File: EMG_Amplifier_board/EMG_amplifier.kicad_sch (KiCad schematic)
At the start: 8 parts, among them J1 Conn_01x04_Socket, J2 Conn_01x04_Pin, J3 Conn_01x06_Pin, J4 Conn_01x06_Socket, J7 Conn_01x06_Pin

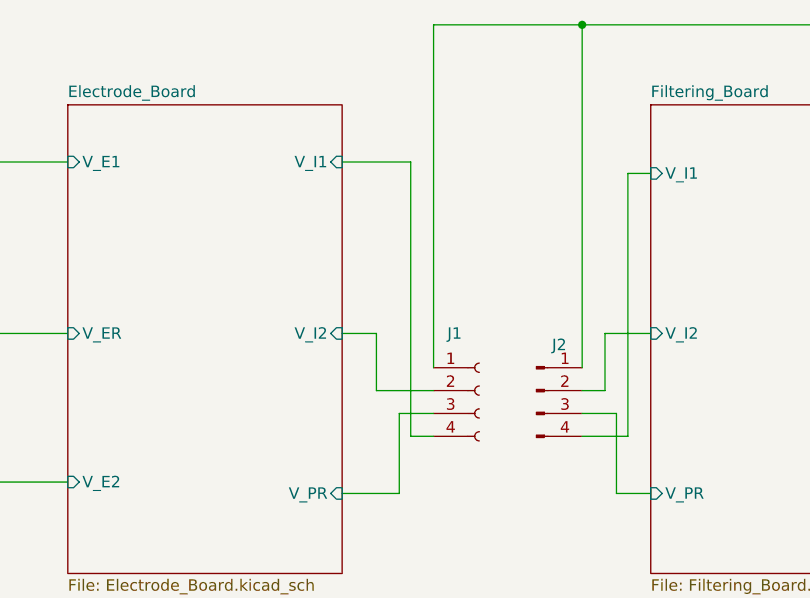
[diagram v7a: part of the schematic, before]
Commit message: correct the 400Hz LPF schematic and InAmp trace routing
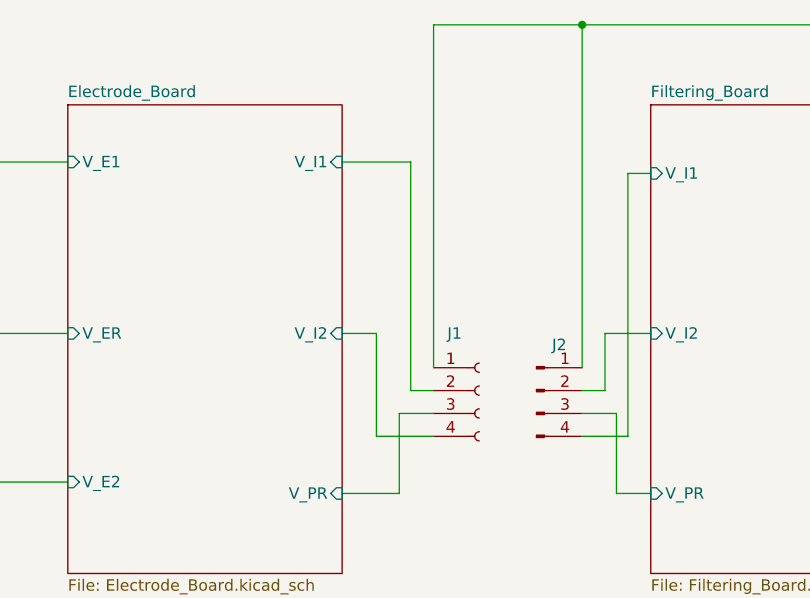
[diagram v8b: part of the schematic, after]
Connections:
- net Electrode_Board/V_I1: now also J1.2 (Pin_2); no longer J1.4 (Pin_4)
- net Electrode_Board/V_I2: now also J1.4 (Pin_4); no longer J1.2 (Pin_2)
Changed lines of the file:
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@@
+	(wire
+		(pts
+			(xy 95.25 69.85) (xy 95.25 95.25)
+		)
+		(stroke
+			(width 0)
+			(type default)
+		)
+	)
 	(wire
 		(pts
@@
 	(wire
 		(pts
-			(xy 95.25 69.85) (xy 95.25 100.33)
-		)
-		(stroke
-			(width 0)
-			(type default)
-		)
-	)
-	(wire
-		(pts
 			(xy 227.33 59.69) (xy 227.33 53.34)
 		)
@@
 	(wire
 		(pts
-			(xy 91.44 88.9) (xy 91.44 95.25)
+			(xy 91.44 88.9) (xy 91.44 100.33)
 		)
 		(stroke
@@
 	(wire
 		(pts
+			(xy 91.44 100.33) (xy 97.79 100.33)
+		)
+		(stroke
+			(width 0)
+			(type default)
+		)
+	)
+	(wire
+		(pts
 			(xy 196.85 104.14) (xy 196.85 91.44)
 		)
@@
 	(wire
 		(pts
-			(xy 91.44 95.25) (xy 97.79 95.25)
-		)
-		(stroke
-			(width 0)
-			(type default)
-		)
-	)
-	(wire
-		(pts
 			(xy 226.06 38.1) (xy 195.58 38.1)
 		)
@@
 	(wire
 		(pts
-			(xy 95.25 100.33) (xy 97.79 100.33)
-		)
-		(stroke
-			(width 0)
-			(type default)
-		)
-	)
-	(wire
-		(pts
 			(xy 195.58 38.1) (xy 195.58 59.69)
 		)
@@
 		)
 		(stroke
+			(width 0)
+			(type default)
+		)
+	)
+	(wire
+		(pts
+			(xy 95.25 95.25) (xy 97.79 95.25)
+		)
+		(stroke
